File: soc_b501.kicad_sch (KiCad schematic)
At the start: 14 parts, among them SW5 SW_Push, U21 XC7Z030_FBG676, U25 SN74LVC1G11DBVR, U26 SN74LVC1G08DBVR

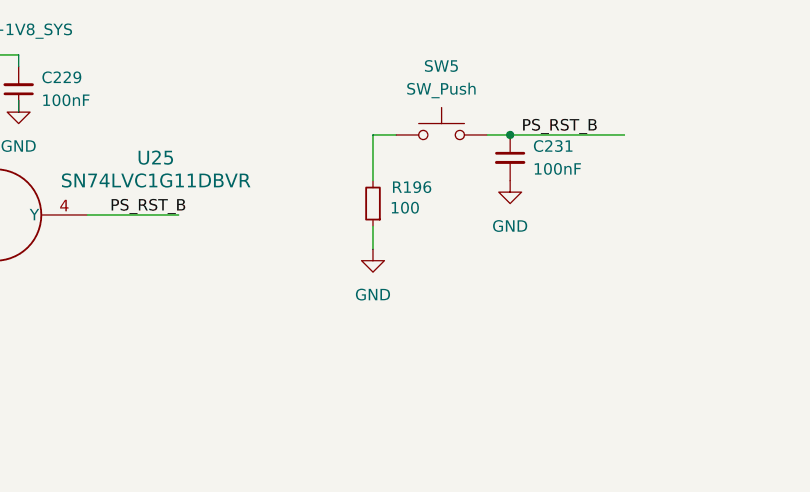
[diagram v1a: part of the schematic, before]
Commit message: schema: JTAG connector & resistors, rev change
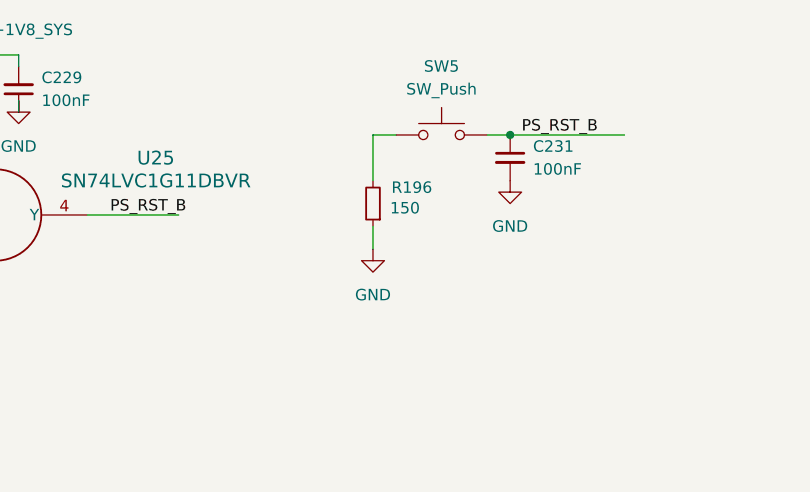
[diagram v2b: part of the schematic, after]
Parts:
- R196: value 100 -> 150; JLCPCB Part # C153111 -> C25082; Part RM04FTN1000 -> 0402WGF1500TCE
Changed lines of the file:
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@@
 		(title "NASR-M")
 		(date "2025-10-22")
-		(rev "D 0.9.5")
+		(rev "D 0.9.8")
 		(company "electrodyssey.net")
 		(comment 1 "PS I2C tree / RTC")
@@
 		(comment 3 "Author: Nazim Aghabayov")
 		(comment 4 "SYZYGY Carrier Mainboard")
-		(comment 5 "rel: Fletched Bustard")
+		(comment 5 "rel: Wild Goose")
 	)
 	(bus_alias "RGMII_BUS"
@@
 			)
 		)
-		(property "Value" "100"
+		(property "Value" "150"
 			(at 117.856 34.798 0)
 			(effects
@@
 			)
 		)
-		(property "JLCPCB Part #" "C153111"
+		(property "JLCPCB Part #" "C25082"
 			(at 114.3 34.29 0)
 			(effects
@@
 			)
 		)
-		(property "Part" "RM04FTN1000"
+		(property "Part" "0402WGF1500TCE"
 			(at 114.3 34.29 90)
 			(effects

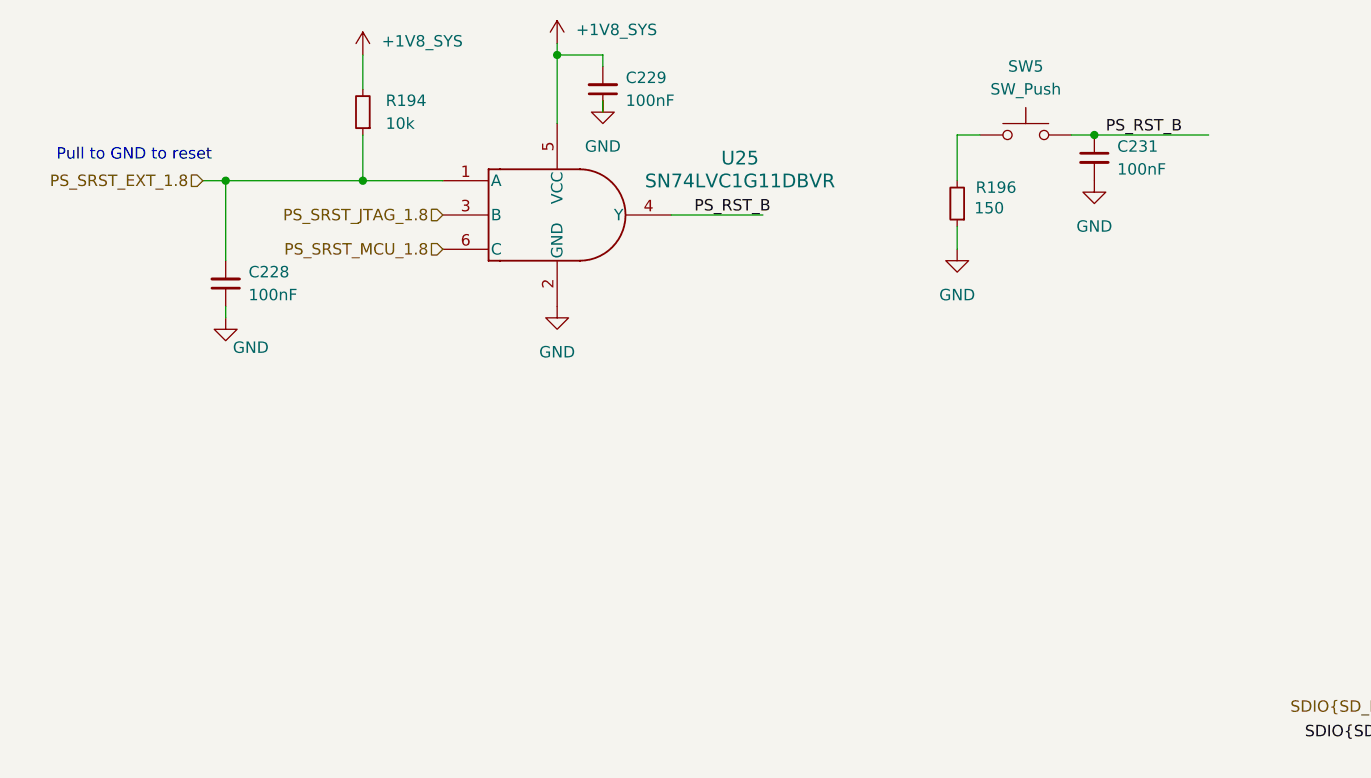
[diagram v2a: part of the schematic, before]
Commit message: schema: PS rst. btn is connected to PS_SRST_EXT_1.8 instead of PS_RST_B
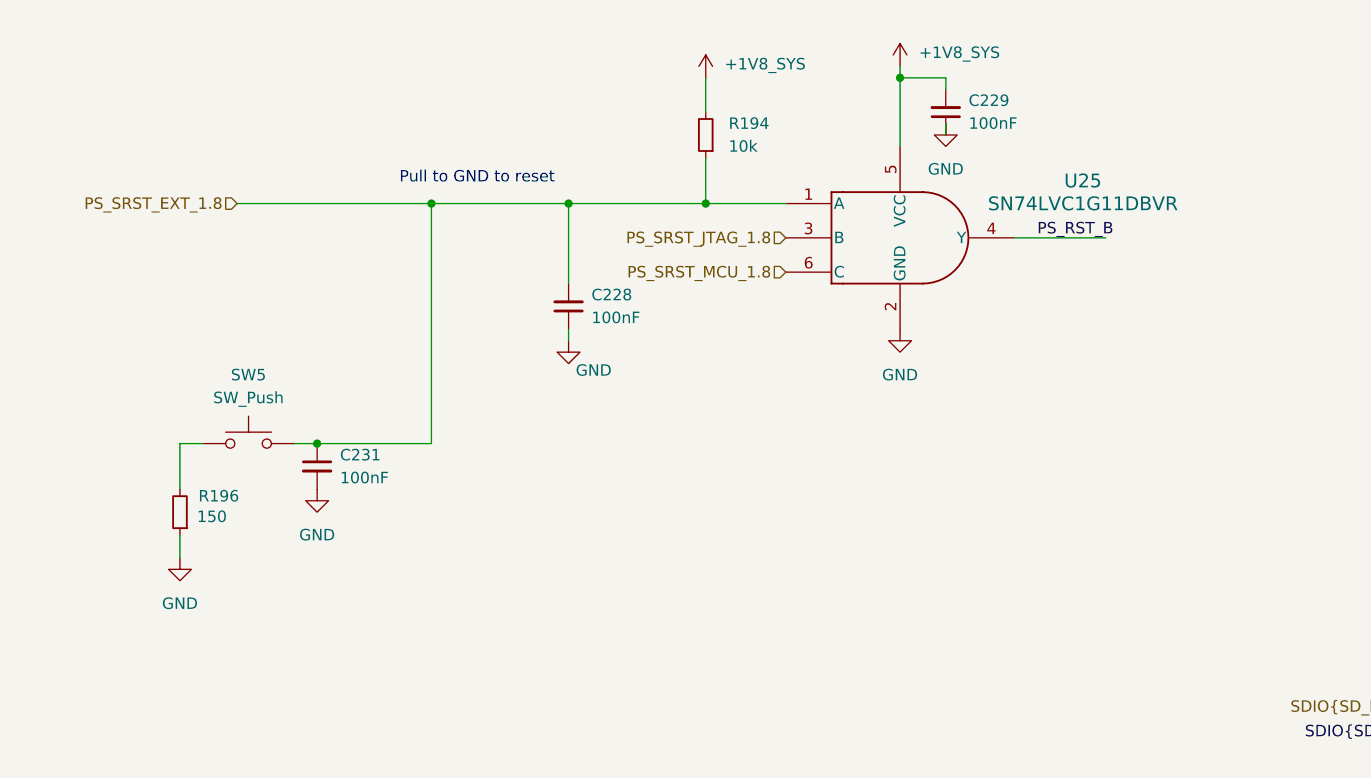
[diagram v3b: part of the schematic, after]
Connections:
- net PS_RST_B: no longer C231.1, SW5.2
- net PS_SRST_EXT_1.8: now also C231.1, SW5.2
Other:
- moved on the sheet: C228, C229, C231, R194, R196, SW5, U25

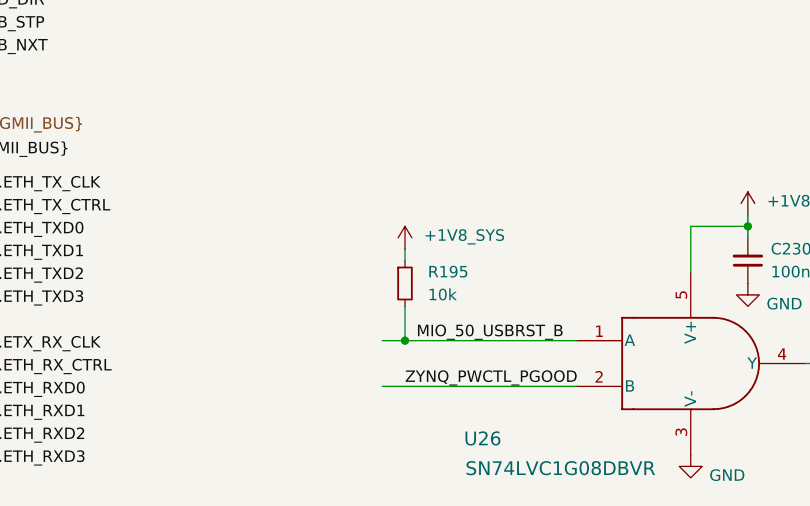
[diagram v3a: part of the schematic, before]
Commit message: schema: don't pull up usb reset by default
mark R195 as DNP
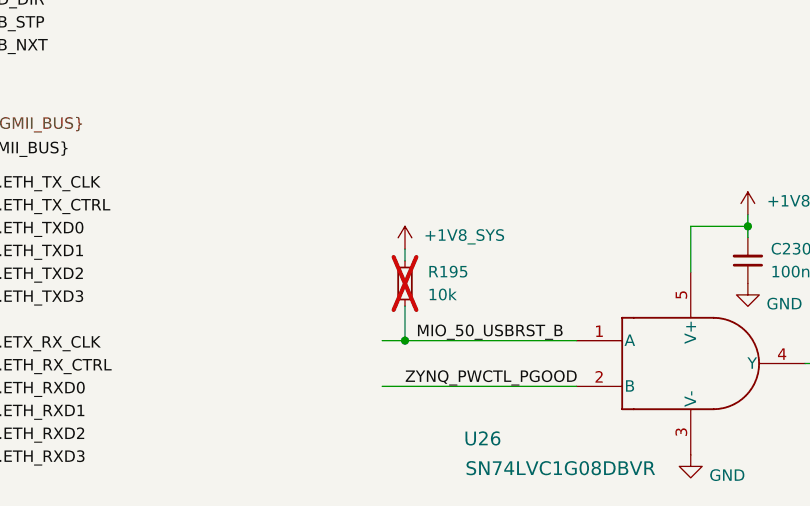
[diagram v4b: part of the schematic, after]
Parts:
- R195: now not fitted
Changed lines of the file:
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@@
 		(in_bom yes)
 		(on_board yes)
-		(dnp no)
+		(dnp yes)
 		(fields_autoplaced yes)
 		(property "Reference" "R195"
